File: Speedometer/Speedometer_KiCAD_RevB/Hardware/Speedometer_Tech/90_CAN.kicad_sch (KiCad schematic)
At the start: 16 parts, among them J900 CTB9302/2, U900 MCP2562FDT-E/SN, U901 MCP2515-I/SO, Y900 ABLS-16.000MHZ-K4T

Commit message: updated troq display with new neopixel
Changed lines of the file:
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@@
 (kicad_sch
-	(version 20231120)
+	(version 20250114)
 	(generator "eeschema")
-	(generator_version "8.0")
+	(generator_version "9.0")
 	(paper "A4")
+	(text "CAN-Filter for D-CAN"
+		(exclude_from_sim no)
+		(at 45.72 93.1672 0)
+		(effects
+			(font
+				(size 1.27 1.27)
+			)
+			(justify left bottom)
+		)
+	)
+	(text "1x MCP2562FDT-E/SN = 10mA"
+		(exclude_from_sim no)
+		(at 129.54 34.7472 0)
+		(effects
+			(font
+				(size 1.27 1.27)
+			)
+			(justify left bottom)
+		)
+	)
+	(text "120r bei can hinzufügen"
+		(exclude_from_sim no)
+		(at 96.52 199.8472 0)
+		(effects
+			(font
+				(size 1.27 1.27)
+			)
+			(justify left bottom)
+		)
+	)
+	(text "CAN Transceiver"
+		(exclude_from_sim no)
+		(at 129.54 98.2472 0)
+		(effects
+			(font
+				(size 1.27 1.27)
+			)
+			(justify left bottom)
+		)
+	)
+	(text "CAN Controller"
+		(exclude_from_sim no)
+		(at 129.54 182.0672 0)
+		(effects
+			(font
+				(size 1.27 1.27)
+			)
+			(justify left bottom)
+		)
+	)
 	(junction
 		(at 35.56 62.6872)
@@
 		)
 	)
-	(text "CAN-Filter for D-CAN"
-		(exclude_from_sim no)
-		(at 45.72 93.1672 0)
-		(effects
-			(font
-				(size 1.27 1.27)
-			)
-			(justify left bottom)
-		)
-	)
-	(text "1x MCP2562FDT-E/SN = 10mA"
-		(exclude_from_sim no)
-		(at 129.54 34.7472 0)
-		(effects
-			(font
-				(size 1.27 1.27)
-			)
-			(justify left bottom)
-		)
-	)
-	(text "120r bei can hinzufügen"
-		(exclude_from_sim no)
-		(at 96.52 199.8472 0)
-		(effects
-			(font
-				(size 1.27 1.27)
-			)
-			(justify left bottom)
-		)
-	)
-	(text "CAN Transceiver"
-		(exclude_from_sim no)
-		(at 129.54 98.2472 0)
-		(effects
-			(font
-				(size 1.27 1.27)
-			)
-			(justify left bottom)
-		)
-	)
-	(text "CAN Controller"
-		(exclude_from_sim no)
-		(at 129.54 182.0672 0)
-		(effects
-			(font
-				(size 1.27 1.27)
-			)
-			(justify left bottom)
-		)
-	)
 	(label "RXCAN"
 		(at 185.42 138.8872 0)
-		(fields_autoplaced yes)
 		(effects
 			(font
@@
 	(label "CAN_H"
 		(at 88.9 88.0872 0)
-		(fields_autoplaced yes)
 		(effects
 			(font
@@
 	(label "CAN_H"
 		(at 223.52 52.5272 0)
-		(fields_autoplaced yes)
 		(effects
 			(font
@@
 	(label "TXCAN"
 		(at 175.26 62.6872 0)
-		(fields_autoplaced yes)
 		(effects
 			(font
@@
 	(label "CAN_L"
 		(at 223.52 62.6872 0)
-		(fields_autoplaced yes)
 		(effects
 			(font
@@
 	(label "SCLK"
 		(at 187.96 143.9672 0)
-		(fields_autoplaced yes)
 		(effects
 			(font
@@
 	(label "CAN_L"
 		(at 88.9 52.5272 0)
-		(fields_autoplaced yes)
 		(effects
 			(font
@@
 	(label "RXCAN"
 		(at 175.26 72.8472 0)
-		(fields_autoplaced yes)
 		(effects
 			(font
@@
 	(label "V-CAN_H"
 		(at 25.4 80.4672 0)
-		(fields_autoplaced yes)
 		(effects
 			(font
@@
 	(label "V-CAN_L"
 		(at 25.4 62.6872 0)
-		(fields_autoplaced yes)
 		(effects
 			(font
@@
 	(label "TXCAN"
 		(at 243.84 143.9672 0)
-		(fields_autoplaced yes)
 		(effects
 			(font
@@
 		(shape passive)
 		(at 251.46 151.5872 180)
-		(fields_autoplaced yes)
 		(effects
 			(font
@@
 		(shape passive)
 		(at 195.58 161.7472 180)
-		(fields_autoplaced yes)
 		(effects
 			(font
@@
 		(shape passive)
 		(at 251.46 133.8072 180)
-		(fields_autoplaced yes)
 		(effects
 			(font
@@
 		(shape input)
 		(at 195.58 149.0472 180)
-		(fields_autoplaced yes)
 		(effects
 			(font
@@
 		(on_board yes)
 		(dnp no)
-		(property "Reference" "#PWR?"
+		(property "Reference" "#PWR0235"
 			(at 106.68 70.3072 0)
 			(effects
@@
 			(project ""
 				(path "/7a911dfa-7957-409a-ad31-10c26a0bf949/b38a2589-c423-411c-a19f-0b86ec6c154c"
-					(reference "#PWR?")
+					(reference "#PWR0235")
 					(unit 1)
 				)
@@
 		(on_board yes)
 		(dnp no)
-		(property "Reference" "#PWR?"
+		(property "Reference" "#PWR0245"
 			(at 165.1 123.6472 0)
 			(effects
@@
 			(project ""
 				(path "/7a911dfa-7957-409a-ad31-10c26a0bf949/b38a2589-c423-411c-a19f-0b86ec6c154c"
-					(reference "#PWR?")
+					(reference "#PWR0245")
 					(unit 1)
 				)
@@
 		(on_board yes)
 		(dnp no)
-		(property "Reference" "#PWR?"
+		(property "Reference" "#PWR0243"
 			(at 78.74 70.3072 0)
 			(effects
@@
 			(project ""
 				(path "/7a911dfa-7957-409a-ad31-10c26a0bf949/b38a2589-c423-411c-a19f-0b86ec6c154c"
-					(reference "#PWR?")
+					(reference "#PWR0243")
 					(unit 1)
 				)
@@
 		(on_board yes)
 		(dnp no)
-		(property "Reference" "#PWR?"
+		(property "Reference" "#PWR0237"
 			(at 152.4 65.2272 0)
 			(effects
@@
 			(project ""
 				(path "/7a911dfa-7957-409a-ad31-10c26a0bf949/b38a2589-c423-411c-a19f-0b86ec6c154c"
-					(reference "#PWR?")
+					(reference "#PWR0237")
 					(unit 1)
 				)
@@
 		(on_board yes)
 		(dnp no)
-		(property "Reference" "#PWR?"
+		(property "Reference" "#PWR0244"
 			(at 185.42 75.3872 0)
 			(effects
@@
 			(project ""
 				(path "/7a911dfa-7957-409a-ad31-10c26a0bf949/b38a2589-c423-411c-a19f-0b86ec6c154c"
-					(reference "#PWR?")
+					(reference "#PWR0244")
 					(unit 1)
 				)
@@
 		(on_board yes)
 		(dnp no)
-		(property "Reference" "#PWR?"
+		(property "Reference" "#PWR0242"
 			(at 241.3 161.7472 0)
 			(effects
@@
 			(project ""
 				(path "/7a911dfa-7957-409a-ad31-10c26a0bf949/b38a2589-c423-411c-a19f-0b86ec6c154c"
-					(reference "#PWR?")
+					(reference "#PWR0242")
 					(unit 1)
 				)
@@
 		(on_board yes)
 		(dnp no)
-		(property "Reference" "#PWR?"
+		(property "Reference" "#PWR0240"
 			(at 223.52 75.3872 0)
 			(effects
@@
 			(project ""
 				(path "/7a911dfa-7957-409a-ad31-10c26a0bf949/b38a2589-c423-411c-a19f-0b86ec6c154c"
-					(reference "#PWR?")
+					(reference "#PWR0240")
 					(unit 1)
 				)
@@
 		(on_board yes)
 		(dnp no)
-		(property "Reference" "#PWR?"
+		(property "Reference" "#PWR0246"
 			(at 165.1 131.2672 0)
 			(effects
@@
 			(project ""
 				(path "/7a911dfa-7957-409a-ad31-10c26a0bf949/b38a2589-c423-411c-a19f-0b86ec6c154c"
-					(reference "#PWR?")
+					(reference "#PWR0246")
 					(unit 1)
 				)
@@
 		(on_board yes)
 		(dnp no)
-		(property "Reference" "#PWR?"
+		(property "Reference" "#PWR0236"
 			(at 160.02 65.2272 0)
 			(effects
@@
 			(project ""
 				(path "/7a911dfa-7957-409a-ad31-10c26a0bf949/b38a2589-c423-411c-a19f-0b86ec6c154c"
-					(reference "#PWR?")
+					(reference "#PWR0236")
 					(unit 1)
 				)
@@
 		(on_board yes)
 		(dnp no)
-		(property "Reference" "#PWR?"
+		(property "Reference" "#PWR0247"
 			(at 157.48 169.3672 0)
 			(effects
@@
 			(project ""
 				(path "/7a911dfa-7957-409a-ad31-10c26a0bf949/b38a2589-c423-411c-a19f-0b86ec6c154c"
-					(reference "#PWR?")
+					(reference "#PWR0247")
 					(unit 1)
 				)
@@
 		(on_board yes)
 		(dnp no)
-		(property "Reference" "#PWR?"
+		(property "Reference" "#PWR0238"
 			(at 160.02 52.5272 0)
 			(effects
@@
 			(project ""
 				(path "/7a911dfa-7957-409a-ad31-10c26a0bf949/b38a2589-c423-411c-a19f-0b86ec6c154c"
-					(reference "#PWR?")
+					(reference "#PWR0238")
 					(unit 1)
 				)
@@
 		(on_board yes)
 		(dnp no)
-		(property "Reference" "#PWR?"
+		(property "Reference" "#PWR0239"
 			(at 152.4 52.5272 0)
 			(effects
@@
 			(project ""
 				(path "/7a911dfa-7957-409a-ad31-10c26a0bf949/b38a2589-c423-411c-a19f-0b86ec6c154c"
-					(reference "#PWR?")
+					(reference "#PWR0239")
 					(unit 1)
 				)
@@
 		(on_board yes)
 		(dnp no)
-		(property "Reference" "#PWR?"
+		(property "Reference" "#PWR0241"
 			(at 180.34 169.3672 0)
 			(effects
@@
 			(project ""
 				(path "/7a911dfa-7957-409a-ad31-10c26a0bf949/b38a2589-c423-411c-a19f-0b86ec6c154c"
-					(reference "#PWR?")
+					(reference "#PWR0241")
 					(unit 1)
 				)

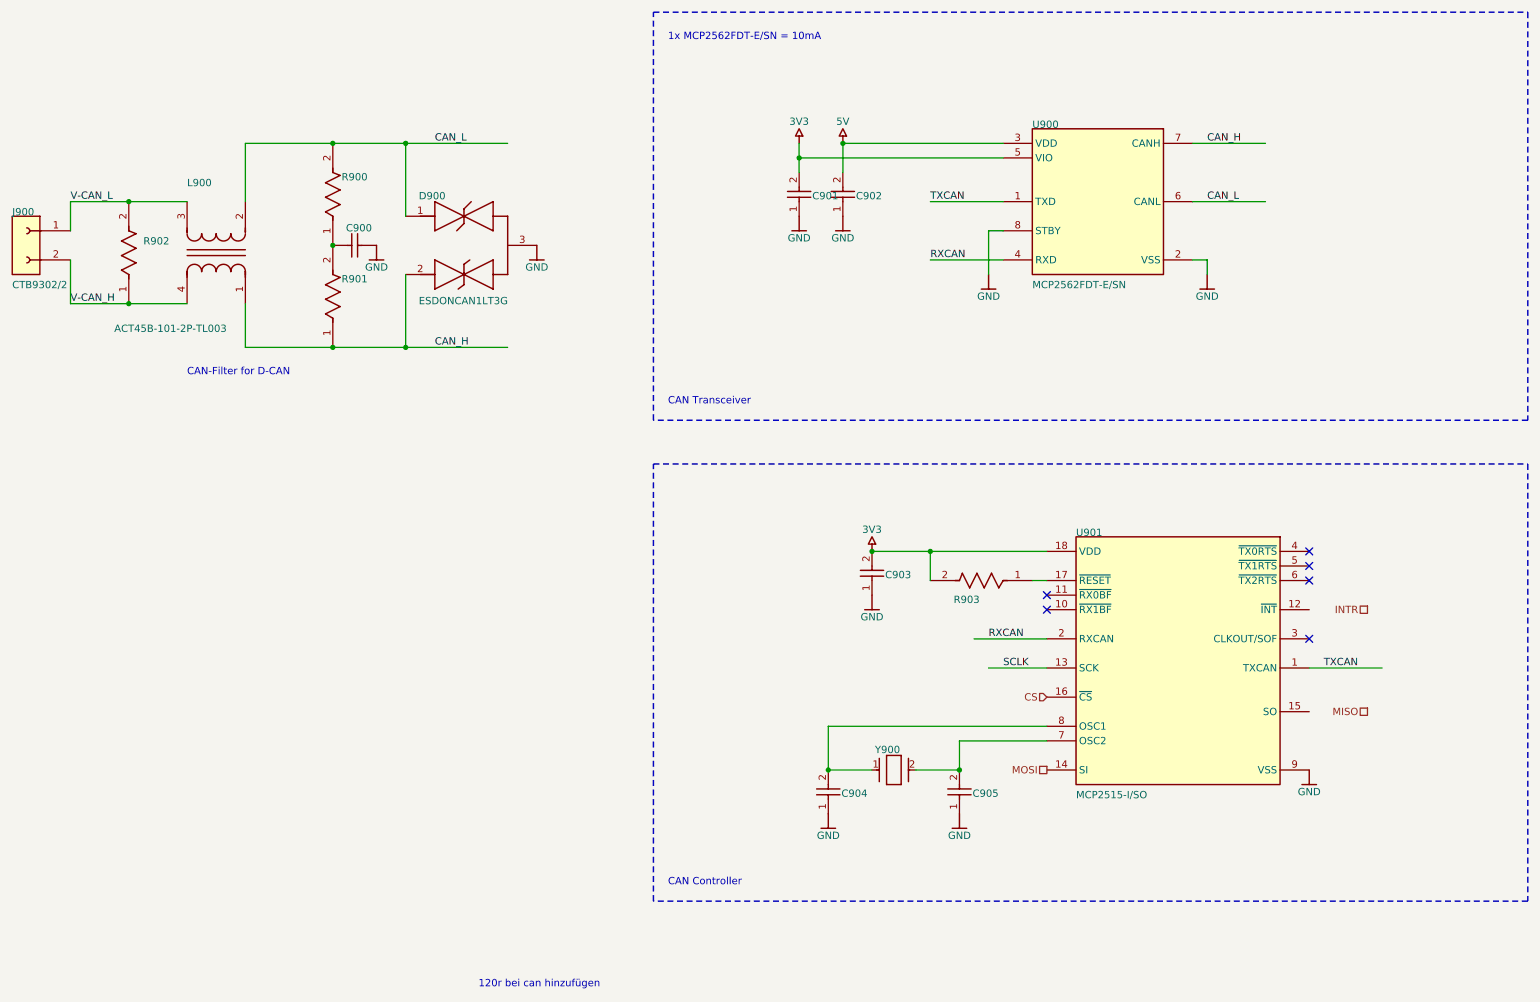
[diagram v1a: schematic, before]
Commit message: current version of lada speedometer in kicad
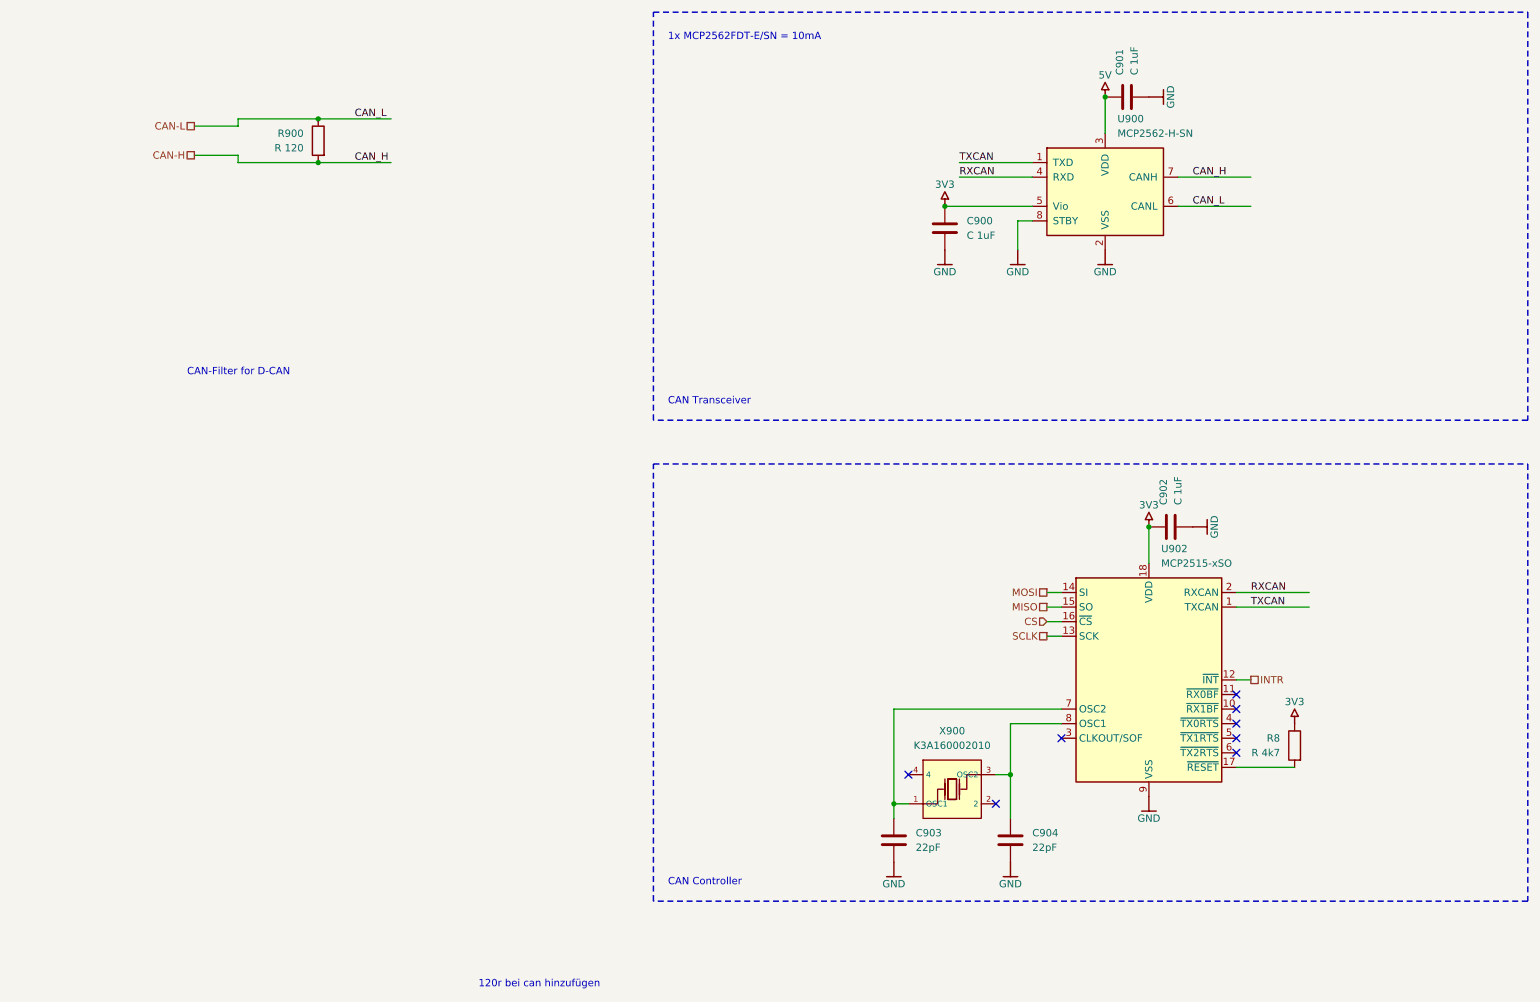
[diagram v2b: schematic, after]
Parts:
- removed C900: GRM188R71H472KA01D, CAPC1608X90X35ML10T15, symbol Speedometer_Tech-altium-import:Designator_0_CAP_0
- removed C901, C902, C903: GRM188R71H104KA93D, CAPC1608X90X35ML10T15, symbol Speedometer_Tech-altium-import:Designator_1_CAP-NP-2
- removed C904, C905: GRM1885C1H220JA01D, CAPC1608X90X35ML10T15, symbol Speedometer_Tech-altium-import:Designator_1_CAP-NP-2
- removed D900: ESDONCAN1LT3G, FP-318-MFG, symbol Speedometer_Tech-altium-import:Designator_0_1bf5749f910b55743977e6066da6fbb
- removed J900: CTB9302/2, CTB9302-2, symbol Speedometer_Tech-altium-import:Designator_0_CTB9302-2
- removed L900: ACT45B-101-2P-TL003, FP-ACT45B-MFG, symbol Speedometer_Tech-altium-import:Designator_1_7eaeb7798601bc1e7f00a291f87c402
- removed R900, R901: CRCW06034K70FKEA, FP-CRCW0603-e3-IPC_A, symbol Speedometer_Tech-altium-import:Designator_1_1029c3af85768c4190bb7ad29bc67b5
- removed R902: CRCW0603120RFKEA, FP-CRCW0603-e3-MFG, symbol Speedometer_Tech-altium-import:Designator_1_1029c3af85768c4190bb7ad29bc67b5
- removed R903: CRCW06034K70FKEA, FP-CRCW0603-e3-IPC_A, symbol Speedometer_Tech-altium-import:Designator_2_1029c3af85768c4190bb7ad29bc67b5
- removed U900: MCP2562FDT-E/SN, FP-C04-057-SN-MFG, symbol Speedometer_Tech-altium-import:Designator_0_fcb6c66e4429206983adab9201371df
- removed U901: MCP2515-I/SO, FP-C04-051-MFG, symbol Speedometer_Tech-altium-import:Designator_0_1c78ea6ff576bac94664e2637e1b479
- removed Y900: ABLS-16.000MHZ-K4T, FP-ABLS-MFG, symbol Speedometer_Tech-altium-import:Designator_0_c23a69dc6c9e2f18f2079038eb95dd1
- added C900, C901, C902: C 1uF, Capacitor_SMD:C_0603_1608Metric, symbol Device:C
- added C903, C904: 22pF, Capacitor_SMD:C_0603_1608Metric, symbol Device:C
- added R8: R 4k7, Resistor_SMD:R_0603_1608Metric, symbol Device:R
- added R900: R 120, Resistor_SMD:R_0603_1608Metric, symbol Device:R
- added U900: MCP2562-H-SN, Package_SO:SOIC-8_3.9x4.9mm_P1.27mm, symbol Interface_CAN_LIN:MCP2562-H-SN
- added U902: MCP2515-xSO, Package_SO:SOIC-18W_7.5x11.6mm_P1.27mm, symbol Interface_CAN_LIN:MCP2515-xSO
- added X900: K3A160002010, footprint:CRYSTAL-SMD_4P-L3.2-W2.5-BL, symbol K3A160002010:K3A160002010
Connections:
- net 3V3: now also C900.1, C902.1, R8.1, U900.5 (Vio), U902.18 (VDD)
- net 5V: now also C901.1, U900.3 (VDD)
- net CS: now also U902.16 (~{CS})
- net GND: now also C900.2, C901.2, C902.2, C903.2, C904.2, U900.2 (VSS), U900.8 (STBY), U902.9 (VSS)
- net INTR: now also U902.12 (~{INT})
- net MISO: now also U902.15 (SO)
- net MOSI: now also U902.14 (SI)
- net RXCAN: now also U900.4 (RXD), U902.2 (RXCAN)
- net SCLK: now also U902.13 (SCK)
- net TXCAN: now also U900.1 (TXD), U902.1 (TXCAN)
- new net: R8.2, U902.17 (~{RESET})
- new net: C903.1, U902.7 (OSC2), X900.1 (OSC1)
- new net: C904.1, U902.8 (OSC1), X900.3 (OSC2)
- new net CAN-H: R900.2, U900.7 (CANH)
- new net CAN-L: R900.1, U900.6 (CANL)
- no-connect marks 6 -> 8

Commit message: Speedometer DRC mostly passed
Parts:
- X900: footprint footprint:CRYSTAL-SMD_4P-L3.2-W2.5-BL -> Crystal:Crystal_SMD_3225-4Pin_3.2x2.5mm
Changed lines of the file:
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@@
 			)
 		)
-		(property "Description" ""
+		(property "Description" "Power symbol creates a global label with name '5V'"
 			(at 238.76 153.67 0)
 			(effects
@@
 			)
 		)
-		(property "Description" ""
+		(property "Description" "Power symbol creates a global label with name 'GND'"
 			(at 168.91 177.8 0)
 			(effects
@@
 			)
 		)
-		(property "Description" ""
+		(property "Description" "Power symbol creates a global label with name 'GND'"
 			(at 177.8 71.12 0)
 			(effects
@@
 			)
 		)
-		(property "Description" ""
+		(property "Description" "Power symbol creates a global label with name 'GND'"
 			(at 213.36 44.45 0)
 			(effects
@@
 			)
 		)
-		(property "Footprint" "footprint:CRYSTAL-SMD_4P-L3.2-W2.5-BL"
+		(property "Footprint" "Crystal:Crystal_SMD_3225-4Pin_3.2x2.5mm"
 			(at 179.07 175.26 0)
 			(effects
@@
 			)
 		)
-		(property "Description" ""
+		(property "Description" "Power symbol creates a global label with name 'GND'"
 			(at 190.5 71.12 0)
 			(effects
@@
 			)
 		)
-		(property "Description" ""
+		(property "Description" "Power symbol creates a global label with name 'GND'"
 			(at 213.36 166.37 0)
 			(effects
@@
 			)
 		)
-		(property "Description" ""
+		(property "Description" "Power symbol creates a global label with name '5V'"
 			(at 213.36 119.38 0)
 			(effects
@@
 			)
 		)
-		(property "Description" ""
+		(property "Description" "Power symbol creates a global label with name 'GND'"
 			(at 205.74 71.12 0)
 			(effects
@@
 			)
 		)
-		(property "Description" ""
+		(property "Description" "Power symbol creates a global label with name 'GND'"
 			(at 189.23 177.8 0)
 			(effects
@@
 			)
 		)
-		(property "Description" ""
+		(property "Description" "Power symbol creates a global label with name '5V'"
 			(at 205.74 44.45 0)
 			(effects
@@
 			)
 		)
-		(property "Description" ""
+		(property "Description" "Power symbol creates a global label with name 'GND'"
 			(at 220.98 119.38 0)
 			(effects
@@
 			)
 		)
-		(property "Description" ""
+		(property "Description" "Power symbol creates a global label with name '3V3'"
 			(at 177.8 63.5 0)
 			(effects
